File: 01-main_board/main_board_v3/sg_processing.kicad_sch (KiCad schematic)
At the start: 16 parts, among them IC5 INA827AIDGK, IC7 INA827AIDGK, U2 AD5689RARUZ-RL7

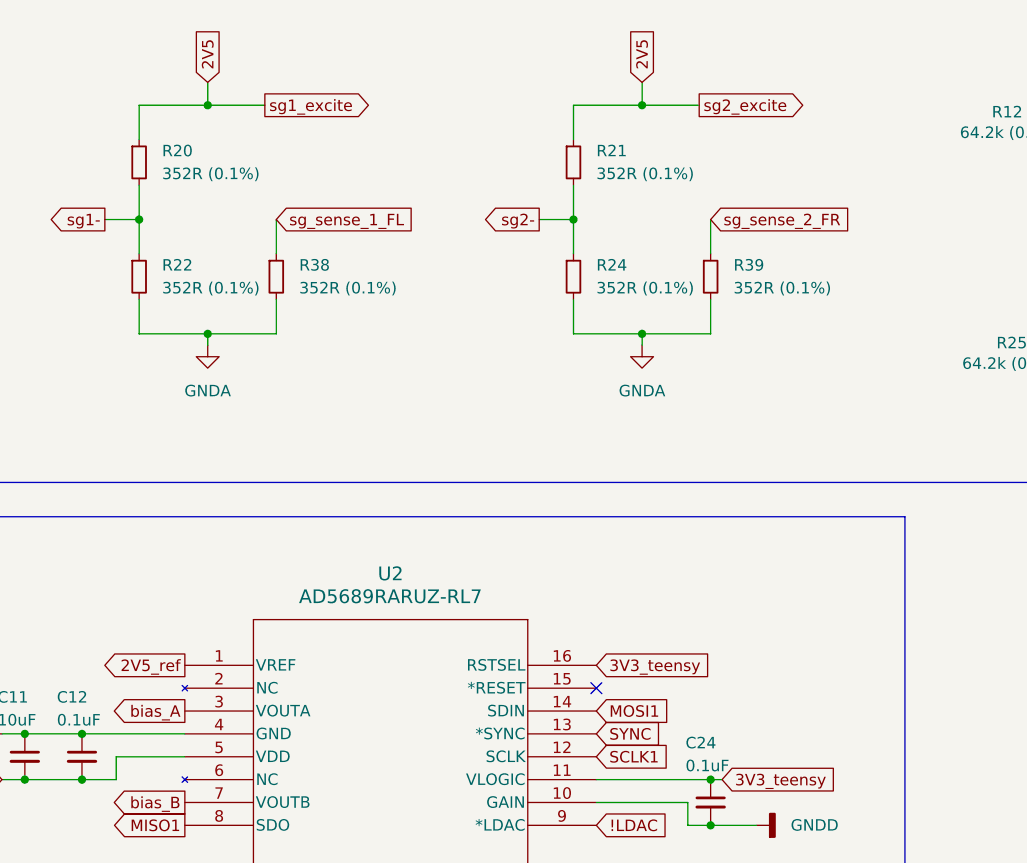
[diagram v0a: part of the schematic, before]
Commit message: changed peripheral connector, addressed slack revisions
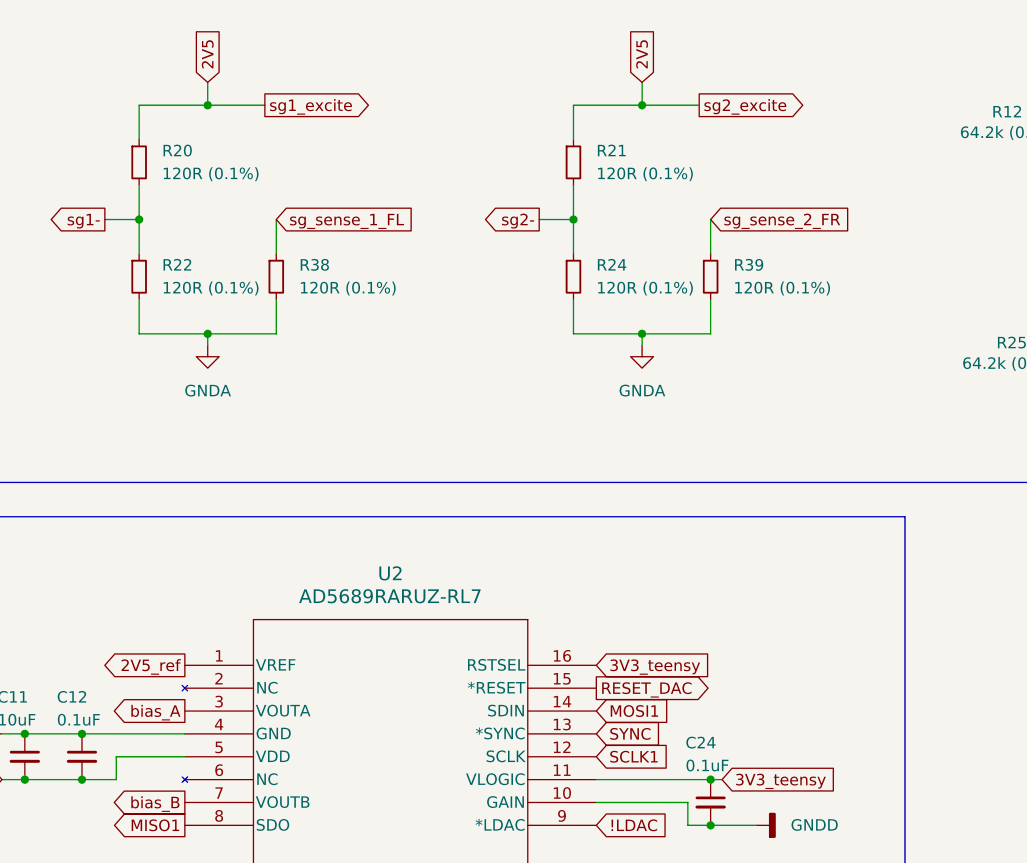
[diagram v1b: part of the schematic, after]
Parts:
- R20, R21, R22, R24, R38, R39: value 352R (0.1%) -> 120R (0.1%)
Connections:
- net RESET_DAC: now reaches U2.15 (*RESET)
- no-connect marks 1 -> 0
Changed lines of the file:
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@@
 		(color 0 0 0 0)
 	)
-	(no_connect
-		(at 132.08 119.38)
-	)
 	(wire
 		(pts
@@
 			(width 0)
 			(type default)
+		)
+	)
+	(global_label "RESET_DAC"
+		(shape output)
+		(at 132.08 119.38 0)
+		(fields_autoplaced yes)
+		(effects
+			(font
+				(size 1.27 1.27)
+			)
+			(justify left)
+		)
+		(property "Intersheetrefs" "${INTERSHEET_REFS}"
+			(at 145.4065 119.38 0)
+			(effects
+				(font
+					(size 1.27 1.27)
+				)
+				(justify left)
+				(hide yes)
+			)
 		)
 	)
@@
 			)
 		)
-		(property "Value" "352R (0.1%)"
+		(property "Value" "120R (0.1%)"
 			(at 83.82 62.2299 0)
 			(effects
@@
 			)
 		)
-		(property "Value" "352R (0.1%)"
+		(property "Value" "120R (0.1%)"
 			(at 147.32 74.9299 0)
 			(effects
@@
 			)
 		)
-		(property "Value" "352R (0.1%)"
+		(property "Value" "120R (0.1%)"
 			(at 99.06 74.9299 0)
 			(effects
@@
 			)
 		)
-		(property "Value" "352R (0.1%)"
+		(property "Value" "120R (0.1%)"
 			(at 83.82 74.9299 0)
 			(effects
@@
 			)
 		)
-		(property "Value" "352R (0.1%)"
+		(property "Value" "120R (0.1%)"
 			(at 132.08 62.2299 0)
 			(effects
@@
 			)
 		)
-		(property "Value" "352R (0.1%)"
+		(property "Value" "120R (0.1%)"
 			(at 132.08 74.9299 0)
 			(effects

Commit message: finished silkscreen + 3D models
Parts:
- C11: footprint Capacitor_SMD:C_0402_1005Metric -> Capacitor_SMD:C_0603_1608Metric
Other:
- note added: "Instrumentation Amplifiers (gain approx = 6.46)"
- note removed: "Instrumentation Amplifiers"
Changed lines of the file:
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@@
 		)
 	)
-	(text "Instrumentation Amplifiers\n"
+	(text "Instrumentation Amplifiers\n(gain approx = 6.46)"
 		(exclude_from_sim no)
 		(at 207.01 90.678 0)
@@
 			)
 		)
-		(property "Footprint" "Capacitor_SMD:C_0402_1005Metric"
+		(property "Footprint" "Capacitor_SMD:C_0603_1608Metric"
 			(at 68.58 127 0)
 			(effects

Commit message: updated 3d models
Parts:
- R12, R25: value 64.2k (0.1%) -> 80 (0.1%)
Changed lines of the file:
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@@
 			)
 		)
-		(property "Value" "64.2k (0.1%)"
-			(at 172.466 57.658 0)
+		(property "Value" "80 (0.1%)"
+			(at 173.736 58.166 0)
 			(effects
 				(font
@@
 			)
 		)
-		(property "Value" "64.2k (0.1%)"
+		(property "Value" "80 (0.1%)"
 			(at 172.72 83.312 0)
 			(effects
